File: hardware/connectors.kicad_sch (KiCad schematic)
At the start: 8 parts, among them J10 Micro_SD_Card, J11 Mechanical only - N/C, J12 Mechanical only - N/C, J5 SAO1, J6 SAO2, J7 Conn_01x08_Socket, J8 Conn_01x08_Socket, J9 Conn_ARM_SWD_TagConnect_TC203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

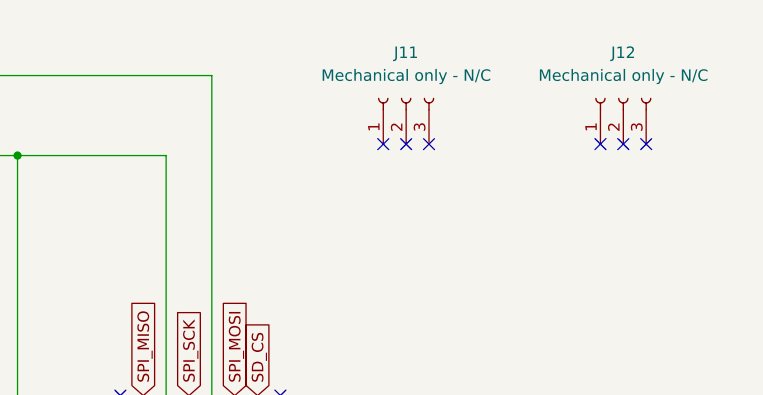
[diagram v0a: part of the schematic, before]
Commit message: add carrier boards for SA818 modules
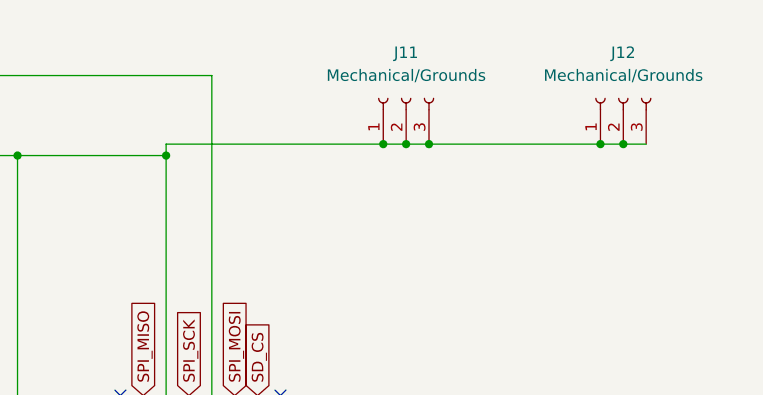
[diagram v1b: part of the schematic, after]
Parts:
- J11, J12: value Mechanical only - N/C -> Mechanical/Grounds
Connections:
- net GND: now also J11.1 (Pin_1), J11.2 (Pin_2), J11.3 (Pin_3), J12.1 (Pin_1), J12.2 (Pin_2), J12.3 (Pin_3)
- no-connect marks 10 -> 4
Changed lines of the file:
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@@
+	)
+	(junction
+		(at 219.71 29.21)
+		(diameter 0)
+		(color 0 0 0 0)
 	)
 	(junction
@@
 	)
 	(junction
+		(at 241.3 29.21)
+		(diameter 0)
+		(color 0 0 0 0)
+	)
+	(junction
+		(at 217.17 29.21)
+		(diameter 0)
+		(color 0 0 0 0)
+	)
+	(junction
 		(at 81.28 21.59)
 		(diameter 0)
@@
 	)
 	(junction
+		(at 214.63 29.21)
+		(diameter 0)
+		(color 0 0 0 0)
+	)
+	(junction
+		(at 238.76 29.21)
+		(diameter 0)
+		(color 0 0 0 0)
+	)
+	(junction
 		(at 113.03 30.48)
 		(diameter 0)
@@
 	)
 	(junction
+		(at 190.5 30.48)
+		(diameter 0)
+		(color 0 0 0 0)
+	)
+	(junction
 		(at 39.37 100.33)
 		(diameter 0)
@@
 	)
 	(no_connect
-		(at 214.63 29.21)
-	)
-	(no_connect
-		(at 217.17 29.21)
-	)
-	(no_connect
-		(at 243.84 29.21)
-	)
-	(no_connect
 		(at 137.16 58.42)
-	)
-	(no_connect
-		(at 241.3 29.21)
-	)
-	(no_connect
-		(at 238.76 29.21)
 	)
 	(no_connect
@@
 		(at 185.42 57.15)
 	)
-	(no_connect
-		(at 219.71 29.21)
-	)
 	(wire
 		(pts
@@
 	(wire
 		(pts
+			(xy 219.71 29.21) (xy 217.17 29.21)
+		)
+		(stroke
+			(width 0)
+			(type default)
+		)
+	)
+	(wire
+		(pts
 			(xy 81.28 21.59) (xy 81.28 52.07)
 		)
@@
 	(wire
 		(pts
+			(xy 190.5 29.21) (xy 190.5 30.48)
+		)
+		(stroke
+			(width 0)
+			(type default)
+		)
+	)
+	(wire
+		(pts
 			(xy 113.03 30.48) (xy 113.03 64.77)
 		)
@@
 	(wire
 		(pts
+			(xy 241.3 29.21) (xy 238.76 29.21)
+		)
+		(stroke
+			(width 0)
+			(type default)
+		)
+	)
+	(wire
+		(pts
 			(xy 170.18 48.26) (xy 170.18 21.59)
 		)
@@
 	(wire
 		(pts
+			(xy 243.84 29.21) (xy 241.3 29.21)
+		)
+		(stroke
+			(width 0)
+			(type default)
+		)
+	)
+	(wire
+		(pts
 			(xy 173.99 100.33) (xy 173.99 30.48)
 		)
@@
 	(wire
 		(pts
+			(xy 217.17 29.21) (xy 214.63 29.21)
+		)
+		(stroke
+			(width 0)
+			(type default)
+		)
+	)
+	(wire
+		(pts
 			(xy 38.1 21.59) (xy 81.28 21.59)
 		)
@@
 	(wire
 		(pts
+			(xy 214.63 29.21) (xy 190.5 29.21)
+		)
+		(stroke
+			(width 0)
+			(type default)
+		)
+	)
+	(wire
+		(pts
 			(xy 161.29 30.48) (xy 173.99 30.48)
 		)
@@
 		(pts
 			(xy 50.8 52.07) (xy 50.8 30.48)
+		)
+		(stroke
+			(width 0)
+			(type default)
+		)
+	)
+	(wire
+		(pts
+			(xy 238.76 29.21) (xy 219.71 29.21)
 		)
 		(stroke
@@
 			)
 		)
-		(property "Value" "Mechanical only - N/C"
+		(property "Value" "Mechanical/Grounds"
 			(at 217.17 21.59 90)
 			(effects
@@
 			)
 		)
-		(property "Value" "Mechanical only - N/C"
+		(property "Value" "Mechanical/Grounds"
 			(at 241.3 21.59 90)
 			(effects

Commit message: add footprints and break carrier boards out into standalone projects
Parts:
- J10: footprint (none) -> Connector_Card:microSD_HC_Molex_104031-0811
- J11, J12: footprint (none) -> Connector_PinSocket_2.54mm:PinSocket_1x03_P2.54mm_Vertical
- J5, J6: footprint (none) -> Connector_PinHeader_2.54mm:PinHeader_2x03_P2.54mm_Vertical
- J7, J8: footprint (none) -> Connector_PinSocket_2.54mm:PinSocket_1x08_P2.54mm_Vertical
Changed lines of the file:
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@@
 			)
 		)
-		(property "Footprint" ""
+		(property "Footprint" "Connector_PinHeader_2.54mm:PinHeader_2x03_P2.54mm_Vertical"
 			(at 43.18 54.61 0)
 			(effects
@@
 			)
 		)
-		(property "Footprint" ""
+		(property "Footprint" "Connector_PinSocket_2.54mm:PinSocket_1x08_P2.54mm_Vertical"
 			(at 41.91 81.28 0)
 			(effects
@@
 			)
 		)
-		(property "Footprint" ""
+		(property "Footprint" "Connector_PinHeader_2.54mm:PinHeader_2x03_P2.54mm_Vertical"
 			(at 86.36 54.61 0)
 			(effects
@@
 			)
 		)
-		(property "Footprint" ""
+		(property "Footprint" "Connector_PinSocket_2.54mm:PinSocket_1x08_P2.54mm_Vertical"
 			(at 72.39 81.28 0)
 			(effects
@@
 			)
 		)
-		(property "Footprint" ""
+		(property "Footprint" "Connector_PinSocket_2.54mm:PinSocket_1x03_P2.54mm_Vertical"
 			(at 217.17 24.13 0)
 			(effects
@@
 			)
 		)
-		(property "Footprint" ""
+		(property "Footprint" "Connector_Card:microSD_HC_Molex_104031-0811"
 			(at 203.2 109.22 0)
 			(effects
@@
 			)
 		)
-		(property "Footprint" ""
+		(property "Footprint" "Connector_PinSocket_2.54mm:PinSocket_1x03_P2.54mm_Vertical"
 			(at 241.3 24.13 0)
 			(effects
